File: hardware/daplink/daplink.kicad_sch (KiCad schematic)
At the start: 33 parts, among them J1 Conn_01x04, J2 Conn_01x05, J3 Conn_01x05, P1 USB_C_Plug_USB2.0, U1 AMS1117-3.3, U2 STM32F103CBTx, Y1 8MHz

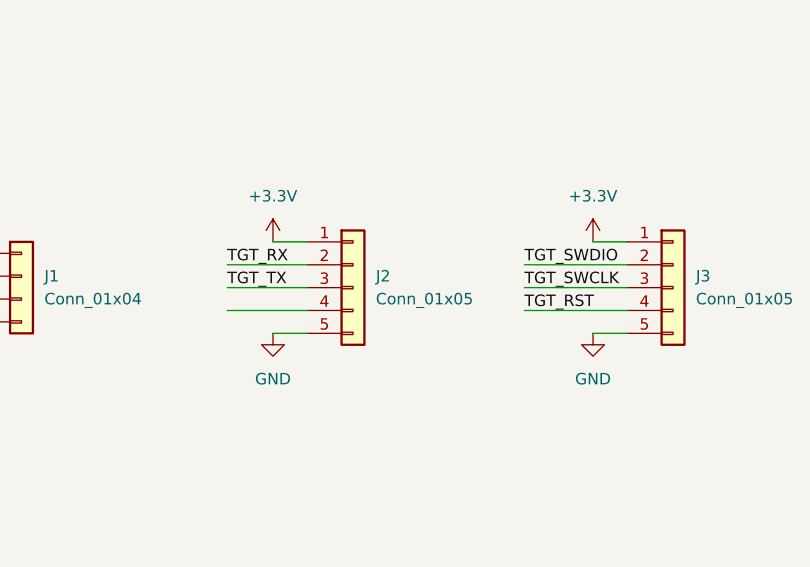
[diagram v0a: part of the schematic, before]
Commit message: feat(hw/schematic): placement and layout
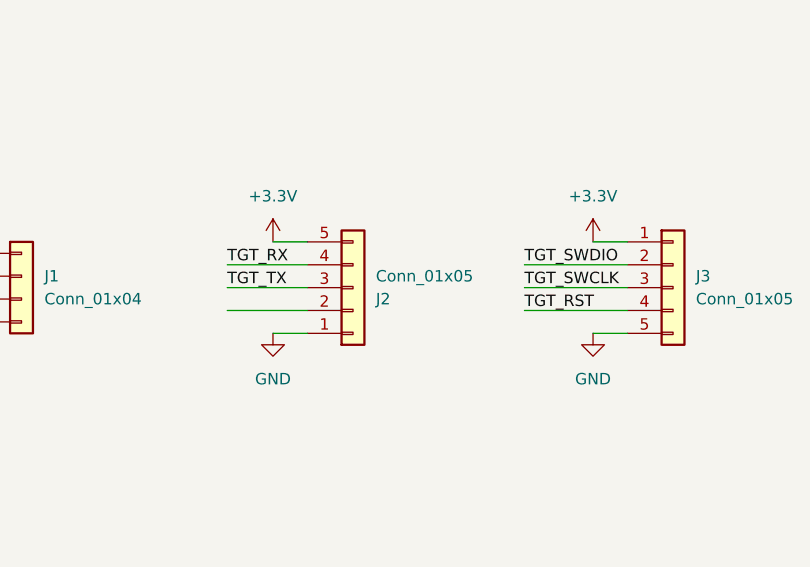
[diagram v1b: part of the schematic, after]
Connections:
- net +3.3V: now also J2.5 (Pin_5); no longer J2.1 (Pin_1)
- net GND: now also J2.1 (Pin_1); no longer J2.5 (Pin_5)
- net TGT_RX: now also J2.4 (Pin_4); no longer J2.2 (Pin_2)
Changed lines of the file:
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@@
     )
   )
-  (symbol (lib_id "Connector_Generic:Conn_01x05") (at 80.01 101.6 0) (unit 1)
+  (symbol (lib_id "Connector_Generic:Conn_01x05") (at 80.01 101.6 0) (mirror x) (unit 1)
     (in_bom yes) (on_board yes) (dnp no) (fields_autoplaced)
-    (property "Reference" "J2" (at 82.55 100.33 0)
+    (property "Reference" "J2" (at 82.55 102.87 0)
       (effects (font (size 1.27 1.27)) (justify left))
     )
-    (property "Value" "Conn_01x05" (at 82.55 102.87 0)
+    (property "Value" "Conn_01x05" (at 82.55 100.33 0)
       (effects (font (size 1.27 1.27)) (justify left))
     )

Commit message: feat(hw/schematic): change the footprint of crystal
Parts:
- removed Y1: 8MHz, Crystal:Crystal_SMD_SeikoEpson_FA238V-4Pin_3.2x2.5mm_HandSoldering, symbol Device:Crystal_GND2_Small
- added Y1: 8MHz, Crystal:Crystal_SMD_5032-2Pin_5.0x3.2mm, symbol Device:Crystal
- C5, C6: value 10nF -> 8pF
- D1: value LED -> LEDB
- D2: value LED -> LEDG
- D3: value LED -> LEDR
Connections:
- net OSCIN: now also Y1.1
- net OSCOUT: now also Y1.2
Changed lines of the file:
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@@
   (junction (at 151.13 78.74) (diameter 0) (color 0 0 0 0)
   )
+  (junction (at 157.48 69.85) (diameter 0) (color 0 0 0 0)
+  )
   (junction (at 153.67 38.1) (diameter 0) (color 0 0 0 0)
   )
+  (junction (at 212.09 31.75) (diameter 0) (color 0 0 0 0)
+  )
+  (junction (at 260.35 135.89) (diameter 0) (color 0 0 0 0)
+  )
+  (junction (at 262.89 74.93) (diameter 0) (color 0 0 0 0)
+  )
+  (junction (at 181.61 95.25) (diameter 0) (color 0 0 0 0)
+  )
+  (junction (at 27.94 66.04) (diameter 0) (color 0 0 0 0)
+  )
+  (junction (at 264.16 125.73) (diameter 0) (color 0 0 0 0)
+  )
+  (junction (at 262.89 36.83) (diameter 0) (color 0 0 0 0)
+  )
+  (junction (at 193.04 128.27) (diameter 0) (color 0 0 0 0)
+  )
+  (junction (at 267.97 87.63) (diameter 0) (color 0 0 0 0)
+  )
+  (junction (at 107.95 48.26) (diameter 0) (color 0 0 0 0)
+  )
+  (junction (at 271.78 74.93) (diameter 0) (color 0 0 0 0)
+  )
+  (junction (at 207.01 31.75) (diameter 0) (color 0 0 0 0)
+  )
+  (junction (at 119.38 38.1) (diameter 0) (color 0 0 0 0)
+  )
+  (junction (at 209.55 110.49) (diameter 0) (color 0 0 0 0)
+  )
+  (junction (at 257.81 123.19) (diameter 0) (color 0 0 0 0)
+  )
   (junction (at 143.51 69.85) (diameter 0) (color 0 0 0 0)
-  )
-  (junction (at 212.09 31.75) (diameter 0) (color 0 0 0 0)
-  )
-  (junction (at 260.35 135.89) (diameter 0) (color 0 0 0 0)
-  )
-  (junction (at 262.89 74.93) (diameter 0) (color 0 0 0 0)
-  )
-  (junction (at 181.61 95.25) (diameter 0) (color 0 0 0 0)
-  )
-  (junction (at 27.94 66.04) (diameter 0) (color 0 0 0 0)
-  )
-  (junction (at 264.16 125.73) (diameter 0) (color 0 0 0 0)
-  )
-  (junction (at 262.89 36.83) (diameter 0) (color 0 0 0 0)
-  )
-  (junction (at 193.04 128.27) (diameter 0) (color 0 0 0 0)
-  )
-  (junction (at 267.97 87.63) (diameter 0) (color 0 0 0 0)
-  )
-  (junction (at 107.95 48.26) (diameter 0) (color 0 0 0 0)
-  )
-  (junction (at 271.78 74.93) (diameter 0) (color 0 0 0 0)
-  )
-  (junction (at 207.01 31.75) (diameter 0) (color 0 0 0 0)
-  )
-  (junction (at 157.48 69.85) (diameter 0) (color 0 0 0 0)
-  )
-  (junction (at 119.38 38.1) (diameter 0) (color 0 0 0 0)
-  )
-  (junction (at 209.55 110.49) (diameter 0) (color 0 0 0 0)
-  )
-  (junction (at 257.81 123.19) (diameter 0) (color 0 0 0 0)
   )
   (no_connect (at 191.77 74.93))
@@
     (stroke (width 0) (type default))
   )
+  (wire (pts (xy 157.48 69.85) (xy 157.48 71.12))
+    (stroke (width 0) (type default))
+  )
   (wire (pts (xy 153.67 38.1) (xy 167.64 38.1))
     (stroke (width 0) (type default))
   )
-  (wire (pts (xy 153.67 69.85) (xy 157.48 69.85))
-    (stroke (width 0) (type default))
-  )
   (wire (pts (xy 224.79 36.83) (xy 236.22 36.83))
     (stroke (width 0) (type default))
@@
     (stroke (width 0) (type default))
   )
-  (wire (pts (xy 157.48 69.85) (xy 157.48 71.12))
-    (stroke (width 0) (type default))
-  )
   (wire (pts (xy 107.95 48.26) (xy 107.95 49.53))
     (stroke (width 0) (type default))
@@
     (stroke (width 0) (type default))
   )
-  (wire (pts (xy 143.51 69.85) (xy 148.59 69.85))
-    (stroke (width 0) (type default))
-  )
   (wire (pts (xy 106.68 96.52) (xy 110.49 96.52))
     (stroke (width 0) (type default))
   )
+  (wire (pts (xy 154.94 69.85) (xy 157.48 69.85))
+    (stroke (width 0) (type default))
+  )
   (wire (pts (xy 106.68 106.68) (xy 110.49 106.68))
     (stroke (width 0) (type default))
@@
     (stroke (width 0) (type default))
   )
-  (wire (pts (xy 143.51 69.85) (xy 143.51 62.23))
+  (wire (pts (xy 143.51 62.23) (xy 143.51 69.85))
     (stroke (width 0) (type default))
   )
@@
     (stroke (width 0) (type default))
   )
-  (wire (pts (xy 143.51 71.12) (xy 143.51 69.85))
-    (stroke (width 0) (type default))
-  )
-  (wire (pts (xy 151.13 72.39) (xy 151.13 78.74))
+  (wire (pts (xy 143.51 69.85) (xy 143.51 71.12))
     (stroke (width 0) (type default))
   )
@@
   )
   (wire (pts (xy 224.79 72.39) (xy 236.22 72.39))
+    (stroke (width 0) (type default))
+  )
+  (wire (pts (xy 147.32 69.85) (xy 143.51 69.85))
     (stroke (width 0) (type default))
   )
@@
       (effects (font (size 1.27 1.27)))
     )
-    (property "Value" "LED" (at 212.09 133.35 0)
+    (property "Value" "LEDG" (at 212.09 133.35 0)
       (effects (font (size 1.27 1.27)))
     )
@@
       (effects (font (size 1.27 1.27)))
     )
-    (property "Value" "LED" (at 270.51 101.6 0)
+    (property "Value" "LEDR" (at 270.51 101.6 0)
       (effects (font (size 1.27 1.27)))
     )
@@
       (effects (font (size 1.27 1.27)) (justify left))
     )
-    (property "Value" "10nF" (at 147.32 76.2 0)
+    (property "Value" "8pF" (at 147.32 76.2 0)
       (effects (font (size 1.27 1.27)) (justify left))
     )
@@
         (path "/514728d6-e60b-46f5-b699-33a1498a2333"
           (reference "C1") (unit 1)
+        )
+      )
+    )
+  )
+  (symbol (lib_id "Device:Crystal") (at 151.13 69.85 0) (unit 1)
+    (in_bom yes) (on_board yes) (dnp no) (fields_autoplaced)
+    (property "Reference" "Y1" (at 151.13 62.23 0)
+      (effects (font (size 1.27 1.27)))
+    )
+    (property "Value" "8MHz" (at 151.13 64.77 0)
+      (effects (font (size 1.27 1.27)))
+    )
+    (property "Footprint" "Crystal:Crystal_SMD_5032-2Pin_5.0x3.2mm" (at 151.13 69.85 0)
+      (effects (font (size 1.27 1.27)) hide)
+    )
+    (property "Datasheet" "~" (at 151.13 69.85 0)
+      (effects (font (size 1.27 1.27)) hide)
+    )
+    (property "JLCPCB" "C5221298" (at 151.13 69.85 0)
+      (effects (font (size 1.27 1.27)) hide)
+    )
+    (pin "1")
+    (pin "2")
+    (instances
+      (project "daplink"
+        (path "/4a115916-3823-4e44-9c09-968e75df0e9b"
+          (reference "Y1") (unit 1)
         )
       )
@@
       (effects (font (size 1.27 1.27)) (justify left))
     )
-    (property "Value" "10nF" (at 161.29 76.2 0)
+    (property "Value" "8pF" (at 161.29 76.2 0)
       (effects (font (size 1.27 1.27)) (justify left))
     )
@@
         (path "/514728d6-e60b-46f5-b699-33a1498a2333"
           (reference "C1") (unit 1)
-        )
-      )
-    )
-  )
-  (symbol (lib_id "Device:Crystal_GND2_Small") (at 151.13 69.85 0) (unit 1)
-    (in_bom yes) (on_board yes) (dnp no) (fields_autoplaced)
-    (property "Reference" "Y1" (at 151.13 63.5 0)
-      (effects (font (size 1.27 1.27)))
-    )
-    (property "Value" "8MHz" (at 151.13 66.04 0)
-      (effects (font (size 1.27 1.27)))
-    )
-    (property "Footprint" "Crystal:Crystal_SMD_SeikoEpson_FA238V-4Pin_3.2x2.5mm_HandSoldering" (at 151.13 69.85 0)
-      (effects (font (size 1.27 1.27)) hide)
-    )
-    (property "Datasheet" "~" (at 151.13 69.85 0)
-      (effects (font (size 1.27 1.27)) hide)
-    )
-    (pin "1")
-    (pin "2")
-    (pin "3")
-    (instances
-      (project "daplink"
-        (path "/4a115916-3823-4e44-9c09-968e75df0e9b"
-          (reference "Y1") (unit 1)
         )
       )
@@
       (effects (font (size 1.27 1.27)))
     )
-    (property "Value" "LED" (at 212.09 125.73 0)
-      (effects (font (size 1.27 1.27)))
-    )
+    (property "Value" "LEDB" (at 212.09 125.73 0)
+      (effects (font (size 1.27 1.27)))
+    )

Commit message: feat(hw/schematic): update jlcpcb lib
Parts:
- C1, C4, C8: JLCPCB (none) -> C57112
- C2, C3: JLCPCB (none) -> C19702
- C5, C6: value 8pF -> 20pF; JLCPCB (none) -> C1648
- C7, C9: JLCPCB (none) -> C1647
- D1: JLCPCB (none) -> C72041
- D2: JLCPCB (none) -> C72043
- D3: JLCPCB (none) -> C2286
- P1: JLCPCB USB-TYPE-C-018 C2927038 -> C2927038/C2927029
- R1, R11, R2, R3, R4: JLCPCB (none) -> C25804
- R10, R5, R9: JLCPCB (none) -> C23162
- R12, R13: JLCPCB (none) -> C23140
- R6, R7: JLCPCB (none) -> C22843
- R8: JLCPCB (none) -> C23179
- U1: JLCPCB (none) -> C6186
- U2: JLCPCB (none) -> C8304
- Y1: JLCPCB C5221298 -> C115962
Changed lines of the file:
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@@
+      (effects (font (size 1.27 1.27)) hide)
+    )
+    (property "JLCPCB" "C25804" (at 54.61 33.02 0)
       (effects (font (size 1.27 1.27)) hide)
     )
@@
     )
     (property "Datasheet" "~" (at 57.15 59.69 0)
+      (effects (font (size 1.27 1.27)) hide)
+    )
+    (property "JLCPCB" "C57112" (at 57.15 59.69 0)
       (effects (font (size 1.27 1.27)) hide)
     )
@@
       (effects (font (size 1.27 1.27)) hide)
     )
+    (property "JLCPCB" "C25804" (at 181.61 54.61 0)
+      (effects (font (size 1.27 1.27)) hide)
+    )
     (pin "1")
     (pin "2")
@@
       (effects (font (size 1.27 1.27)) hide)
     )
+    (property "JLCPCB" "C22843" (at 200.66 135.89 0)
+      (effects (font (size 1.27 1.27)) hide)
+    )
     (pin "1")
     (pin "2")
@@
       (effects (font (size 1.27 1.27)) hide)
     )
+    (property "JLCPCB" "C57112" (at 153.67 41.91 0)
+      (effects (font (size 1.27 1.27)) hide)
+    )
     (pin "1")
     (pin "2")
@@
       (effects (font (size 1.27 1.27)) hide)
     )
+    (property "JLCPCB" "C23162" (at 262.89 40.64 0)
+      (effects (font (size 1.27 1.27)) hide)
+    )
     (pin "1")
     (pin "2")
@@
     )
     (property "Datasheet" "http://www.advanced-monolithic.com/pdf/ds1117.pdf" (at 110.49 44.45 0)
+      (effects (font (size 1.27 1.27)) hide)
+    )
+    (property "JLCPCB" "C6186" (at 107.95 38.1 0)
       (effects (font (size 1.27 1.27)) hide)
     )
@@
       (effects (font (size 1.27 1.27)) hide)
     )
+    (property "JLCPCB" "C23140" (at 269.24 125.73 0)
+      (effects (font (size 1.27 1.27)) hide)
+    )
     (pin "1")
     (pin "2")
@@
     )
     (property "Datasheet" "~" (at 119.38 44.45 0)
+      (effects (font (size 1.27 1.27)) hide)
+    )
+    (property "JLCPCB" "C19702" (at 119.38 44.45 0)
       (effects (font (size 1.27 1.27)) hide)
     )
@@
       (effects (font (size 1.27 1.27)) hide)
     )
+    (property "JLCPCB" "C1647" (at 257.81 132.08 0)
+      (effects (font (size 1.27 1.27)) hide)
+    )
     (pin "1")
     (pin "2")
@@
       (effects (font (size 1.27 1.27)) hide)
     )
+    (property "JLCPCB" "C72043" (at 212.09 135.89 0)
+      (effects (font (size 1.27 1.27)) hide)
+    )
     (pin "1")
     (pin "2")
@@
       (effects (font (size 1.27 1.27)) hide)
     )
+    (property "JLCPCB" "C25804" (at 153.67 33.02 0)
+      (effects (font (size 1.27 1.27)) hide)
+    )
     (pin "1")
     (pin "2")
@@
       (effects (font (size 1.27 1.27)) hide)
     )
+    (property "JLCPCB" "C23162" (at 185.42 95.25 0)
+      (effects (font (size 1.27 1.27)) hide)
+    )
     (pin "1")
     (pin "2")
@@
     )
     (property "Datasheet" "~" (at 262.89 31.75 0)
+      (effects (font (size 1.27 1.27)) hide)
+    )
+    (property "JLCPCB" "C23162" (at 262.89 31.75 0)
       (effects (font (size 1.27 1.27)) hide)
     )
@@
       (effects (font (size 1.27 1.27)) hide)
     )
+    (property "JLCPCB" "C25804" (at 262.89 69.85 0)
+      (effects (font (size 1.27 1.27)) hide)
+    )
     (pin "1")
     (pin "2")
@@
     )
     (property "Datasheet" "~" (at 93.98 44.45 0)
+      (effects (font (size 1.27 1.27)) hide)
+    )
+    (property "JLCPCB" "C19702" (at 93.98 44.45 0)
       (effects (font (size 1.27 1.27)) hide)
     )
@@
       (effects (font (size 1.27 1.27)) hide)
     )
+    (property "JLCPCB" "C2286" (at 270.51 104.14 0)
+      (effects (font (size 1.27 1.27)) hide)
+    )
     (pin "1")
     (pin "2")
@@
       (effects (font (size 1.27 1.27)) hide)
     )
+    (property "JLCPCB" "C22843" (at 200.66 128.27 0)
+      (effects (font (size 1.27 1.27)) hide)
+    )
     (pin "1")
     (pin "2")
@@
       (effects (font (size 1.27 1.27)) (justify left))
     )
-    (property "Value" "8pF" (at 147.32 76.2 0)
+    (property "Value" "20pF" (at 147.32 76.2 0)
       (effects (font (size 1.27 1.27)) (justify left))
     )
@@
       (effects (font (size 1.27 1.27)) hide)
     )
+    (property "JLCPCB" "C1648" (at 143.51 74.93 0)
+      (effects (font (size 1.27 1.27)) hide)
+    )
     (pin "1")
     (pin "2")
@@
       (effects (font (size 1.27 1.27)) hide)
     )
-    (property "JLCPCB" "C5221298" (at 151.13 69.85 0)
+    (property "JLCPCB" "C115962" (at 151.13 69.85 0)
       (effects (font (size 1.27 1.27)) hide)
     )
@@
       (effects (font (size 1.27 1.27)) hide)
     )
+    (property "JLCPCB" "C25804" (at 181.61 41.91 0)
+      (effects (font (size 1.27 1.27)) hide)
+    )
     (pin "1")
     (pin "2")
@@
       (effects (font (size 1.27 1.27)) hide)
     )
-    (property "JLCPCB" "USB-TYPE-C-018 C2927038" (at 35.56 43.18 0)
+    (property "JLCPCB" "C2927038/C2927029" (at 35.56 43.18 0)
       (effects (font (size 1.27 1.27)) hide)
     )
@@
     )
     (property "Datasheet" "https://www.st.com/resource/en/datasheet/stm32f103cb.pdf" (at 207.01 72.39 0)
+      (effects (font (size 1.27 1.27)) hide)
+    )
+    (property "JLCPCB" "C8304" (at 207.01 72.39 0)
       (effects (font (size 1.27 1.27)) hide)
     )
@@
       (effects (font (size 1.27 1.27)) (justify left))
     )
-    (property "Value" "8pF" (at 161.29 76.2 0)
+    (property "Value" "20pF" (at 161.29 76.2 0)
       (effects (font (size 1.27 1.27)) (justify left))
     )
@@
     )
     (property "Datasheet" "~" (at 157.48 74.93 0)
+      (effects (font (size 1.27 1.27)) hide)
+    )
+    (property "JLCPCB" "C1648" (at 157.48 74.93 0)
       (effects (font (size 1.27 1.27)) hide)
     )
@@
       (effects (font (size 1.27 1.27)) hide)
     )
+    (property "JLCPCB" "C23179" (at 259.08 104.14 0)
+      (effects (font (size 1.27 1.27)) hide)
+    )
     (pin "1")
     (pin "2")
@@
       (effects (font (size 1.27 1.27)) hide)
     )
+    (property "JLCPCB" "C72041" (at 212.09 128.27 0)
+      (effects (font (size 1.27 1.27)) hide)
+    )
     (pin "1")
     (pin "2")
@@
       (effects (font (size 1.27 1.27)) hide)
     )
+    (property "JLCPCB" "C23140" (at 269.24 123.19 0)
+      (effects (font (size 1.27 1.27)) hide)
+    )
     (pin "1")
     (pin "2")
@@
     )
     (property "Datasheet" "~" (at 262.89 78.74 0)
+      (effects (font (size 1.27 1.27)) hide)
+    )
+    (property "JLCPCB" "C57112" (at 262.89 78.74 0)
       (effects (font (size 1.27 1.27)) hide)
     )
@@
       (effects (font (size 1.27 1.27)) hide)
     )
+    (property "JLCPCB" "C1647" (at 264.16 132.08 0)
+      (effects (font (size 1.27 1.27)) hide)
+    )

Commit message: fix(hw/sch): fix uart and usb connection
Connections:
- net D+: now also R13.2; no longer R12.2
- net D-: now also R12.2; no longer R13.2
- net TGT_RX: now also J2.3 (Pin_3); no longer J2.4 (Pin_4)
- net TGT_TX: now also J2.4 (Pin_4); no longer J2.3 (Pin_3)
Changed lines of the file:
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@@
-    (effects (font (size 1.27 1.27)) (justify left bottom))
-  )
-  (label "D+" (at 276.86 123.19 0) (fields_autoplaced)
     (effects (font (size 1.27 1.27)) (justify left bottom))
   )
@@
     (effects (font (size 1.27 1.27)) (justify left bottom))
   )
+  (label "D+" (at 276.86 125.73 0) (fields_autoplaced)
+    (effects (font (size 1.27 1.27)) (justify left bottom))
+  )
   (label "OSCIN" (at 180.34 46.99 0) (fields_autoplaced)
     (effects (font (size 1.27 1.27)) (justify left bottom))
   )
   (label "TGT_SWDIO" (at 99.06 99.06 0) (fields_autoplaced)
+    (effects (font (size 1.27 1.27)) (justify left bottom))
+  )
+  (label "TGT_RX" (at 66.04 101.6 0) (fields_autoplaced)
     (effects (font (size 1.27 1.27)) (justify left bottom))
   )
@@
     (effects (font (size 1.27 1.27)) (justify left bottom))
   )
-  (label "TGT_RX" (at 66.04 99.06 0) (fields_autoplaced)
+  (label "D-" (at 276.86 123.19 0) (fields_autoplaced)
     (effects (font (size 1.27 1.27)) (justify left bottom))
   )
@@
     (effects (font (size 1.27 1.27)) (justify left bottom))
   )
-  (label "TGT_TX" (at 66.04 101.6 0) (fields_autoplaced)
-    (effects (font (size 1.27 1.27)) (justify left bottom))
-  )
-  (label "D-" (at 276.86 125.73 0) (fields_autoplaced)
-    (effects (font (size 1.27 1.27)) (justify left bottom))
-  )
   (label "TGT_SWCLK" (at 168.91 97.79 0) (fields_autoplaced)
     (effects (font (size 1.27 1.27)) (justify left bottom))
@@
     (effects (font (size 1.27 1.27)) (justify left bottom))
   )
+  (label "TGT_TX" (at 66.04 99.06 0) (fields_autoplaced)
+    (effects (font (size 1.27 1.27)) (justify left bottom))
+  )

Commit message: fix(hw/sch): fix led and R5
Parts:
- D1: value LEDB -> LEDG
- D2: value LEDG -> LEDB
- R5: value 4K7 -> 100
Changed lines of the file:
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@@
       (effects (font (size 1.27 1.27)))
     )
-    (property "Value" "LEDG" (at 212.09 133.35 0)
+    (property "Value" "LEDB" (at 212.09 133.35 0)
       (effects (font (size 1.27 1.27)))
     )
@@
       (effects (font (size 1.27 1.27)))
     )
-    (property "Value" "4K7" (at 185.42 91.44 90)
+    (property "Value" "100" (at 185.42 91.44 90)
       (effects (font (size 1.27 1.27)))
     )
@@
       (effects (font (size 1.27 1.27)))
     )
-    (property "Value" "LEDB" (at 212.09 125.73 0)
-      (effects (font (size 1.27 1.27)))
-    )
+    (property "Value" "LEDG" (at 212.09 125.73 0)
+      (effects (font (size 1.27 1.27)))
+    )
